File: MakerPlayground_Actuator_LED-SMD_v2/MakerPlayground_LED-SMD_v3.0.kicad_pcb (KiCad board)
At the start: 2 copper layers, 22.5 x 19.9 mm, 4 parts, among them J1 Connector

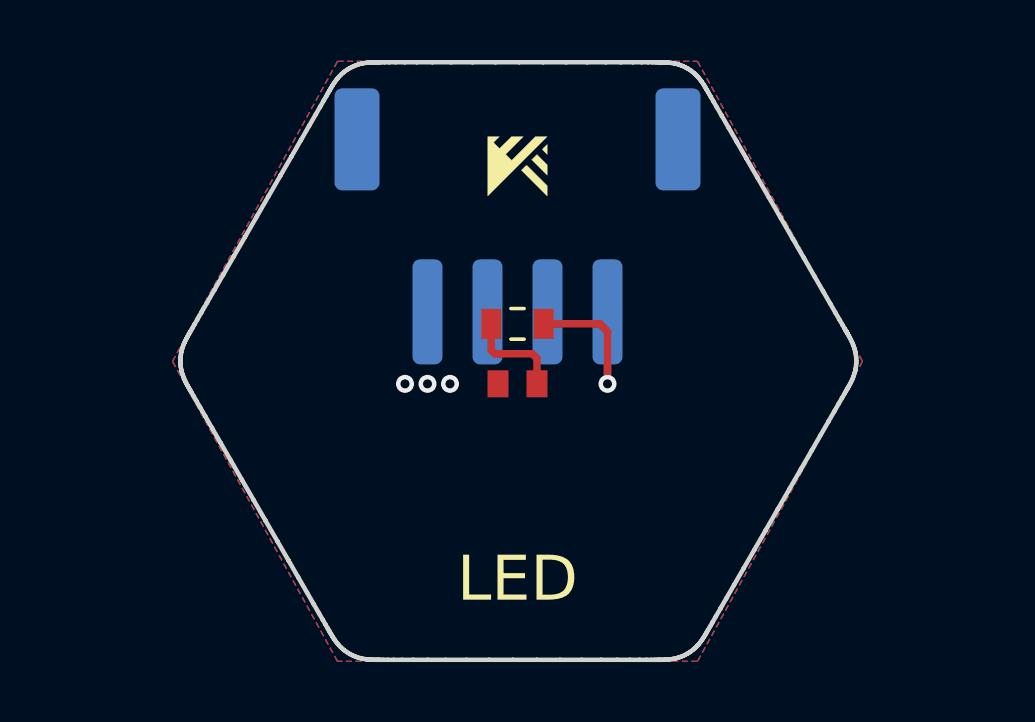
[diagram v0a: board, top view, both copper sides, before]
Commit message: Fix LED-SMD PCB design edge cut and mounting hole.
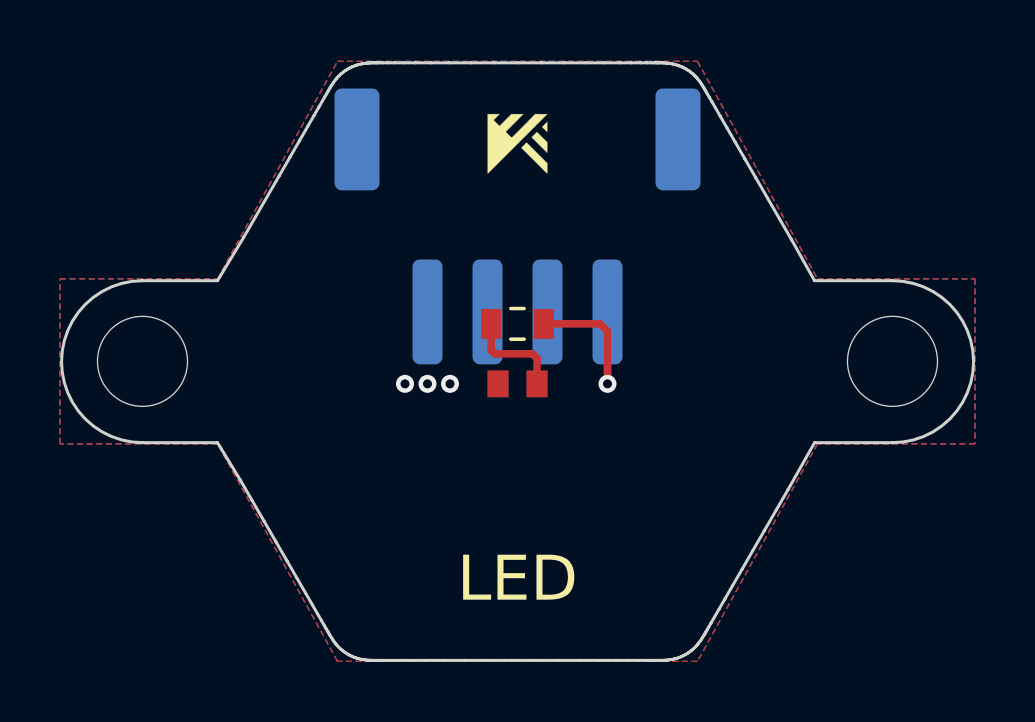
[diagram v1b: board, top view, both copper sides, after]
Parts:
- added REF**: MountingHole_3mm, MountingHole:MountingHole_3mm, F.Cu at (147.5, 101.5)
- added REF**: MountingHole_3mm, MountingHole:MountingHole_3mm, F.Cu at (122.5, 101.5)
- moved G*** 0.75 mm to (135.0, 94.2)
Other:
- board size 22.5 x 19.9 mm -> 30.4 x 19.9 mm

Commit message: Design complete.
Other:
- board text added: "v1.0"
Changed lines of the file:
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@@
   (general
     (thickness 1.6)
-    (drawings 223)
+    (drawings 224)
     (tracks 13)
     (zones 0)
@@
     (pad 1 np_thru_hole circle (at 0 0) (size 3 3) (drill 3) (layers *.Cu *.Mask))
   )
+  (gr_text v1.0 (at 136 110.25) (layer F.SilkS)
+    (effects (font (size 0.5 0.5) (thickness 0.1)))
+  )
   (gr_line (start 139.787 111.468) (end 139.848 111.466) (layer Edge.Cuts) (width 0.1))
